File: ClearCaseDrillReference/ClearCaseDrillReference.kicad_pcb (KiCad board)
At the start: 2 copper layers, 150 x 80 mm, 12 parts

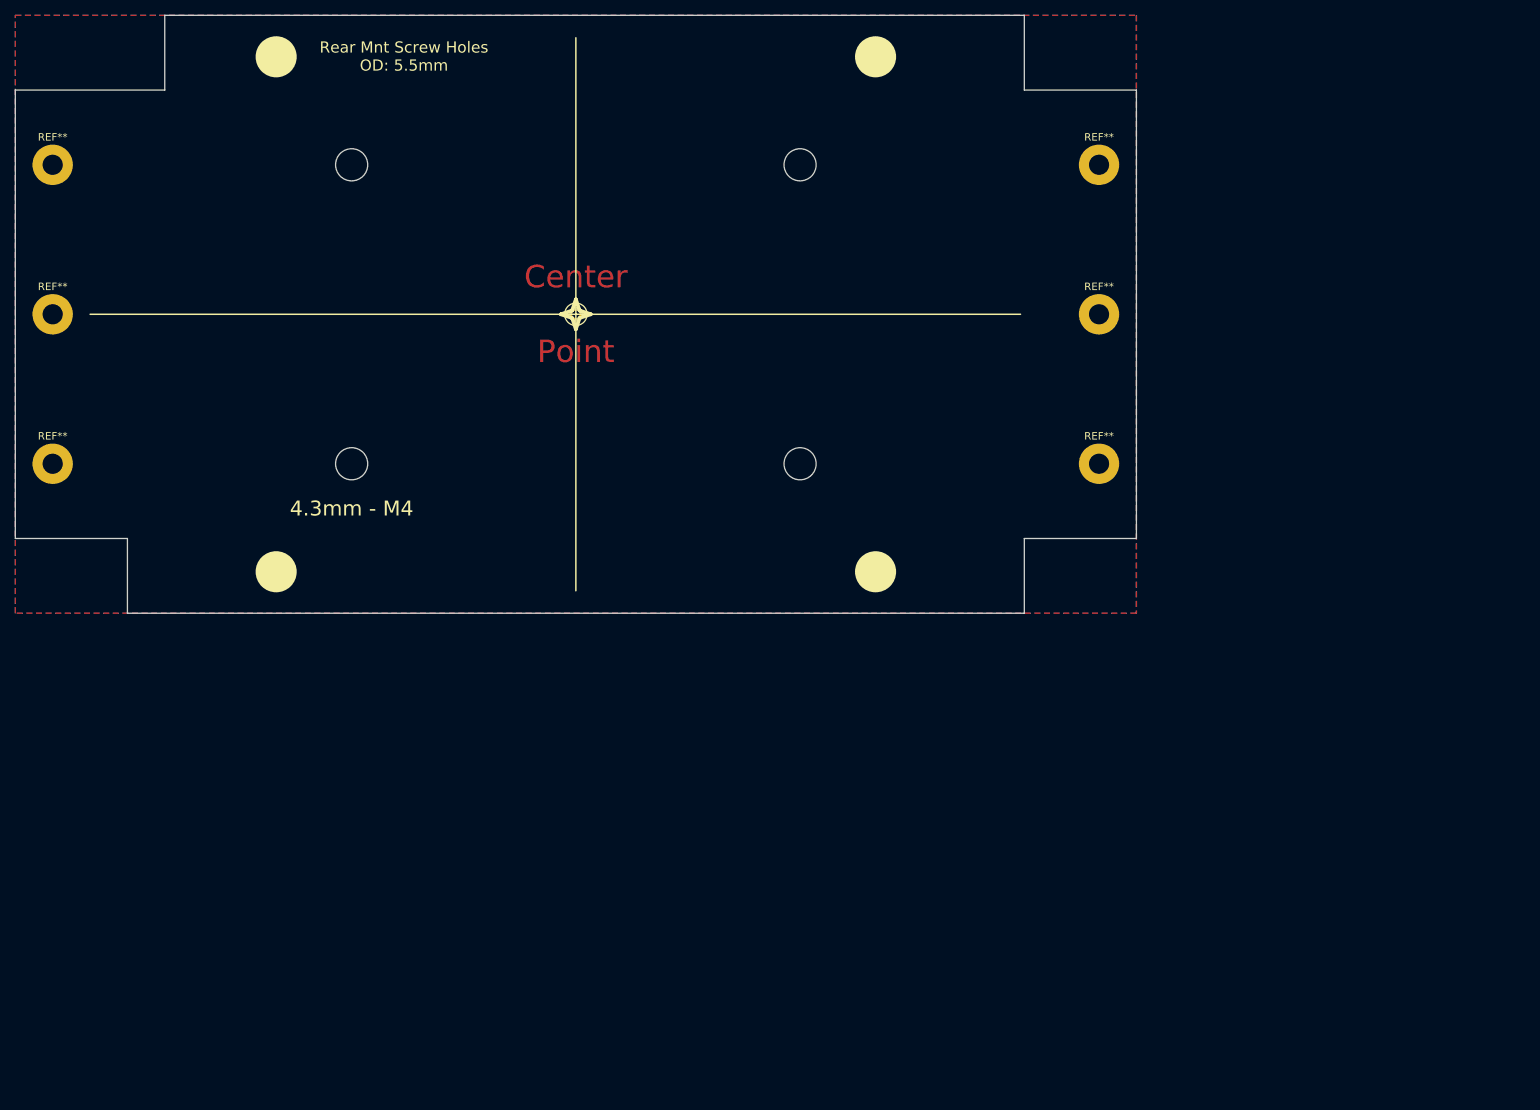
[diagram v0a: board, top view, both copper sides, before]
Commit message: Fix drill reference
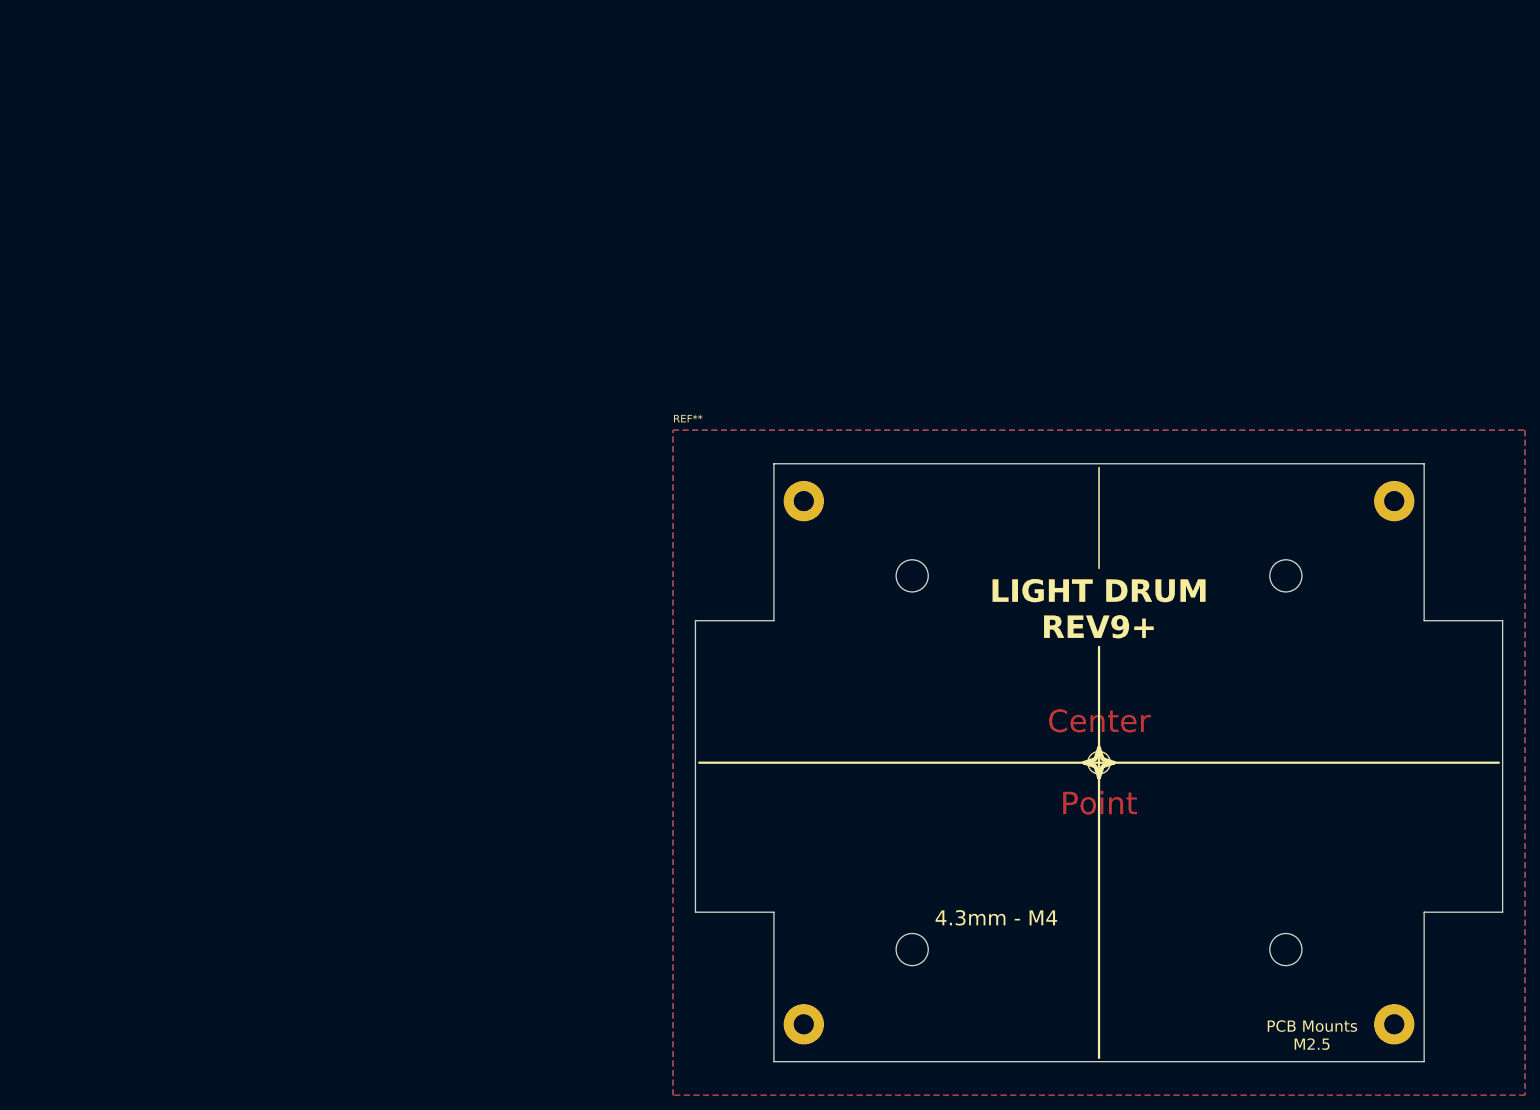
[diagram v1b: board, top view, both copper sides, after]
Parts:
- removed the REF** at (0.00, 0.00)
- removed the REF** at (-70.0, 0.00)
- removed the REF** at (70.0, 0.00)
- added REF**: LeMotech_Black_ENC-115x90, Daxxn_Enclosures:LeMotech_Black_ENC-115x90, F.Cu at (70.0, 60.0)
- moved REF** 125.4 mm to (30.5, 95.0)
- moved REF** 110.1 mm to (30.5, 25.0)
- moved REF** 99.2 mm to (45.0, 85.0)
- moved REF** 93.0 mm to (45.0, 35.0)
- moved REF** 92.2 mm to (70.0, 60.0)
- moved REF** 91.9 mm to (95.0, 85.0)
- moved REF** 85.1 mm to (95.0, 35.0)
- moved REF** 84.8 mm to (109.5, 95.0)
- moved REF** 59.9 mm to (109.5, 25.0)
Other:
- board size 150 x 80 mm -> 108 x 80 mm
- board text added: "LIGHT DRUM REV9+"
- board text added: "PCB Mounts M2.5"
- board text removed: "Rear Mnt Screw Holes OD: 5.5mm"
